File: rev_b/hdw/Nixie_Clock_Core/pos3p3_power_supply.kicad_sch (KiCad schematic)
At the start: 24 parts, among them Q401 BSS214NW, Q402 ZXMS6004FFTA, U401 LT8609A-DD

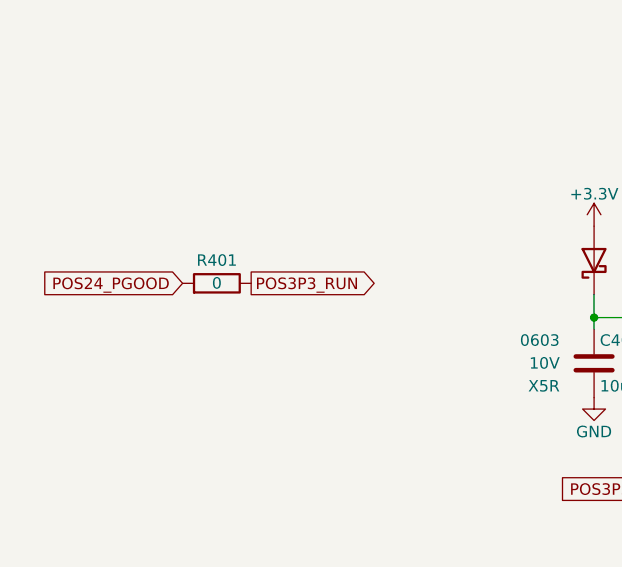
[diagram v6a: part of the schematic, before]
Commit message: added BOM
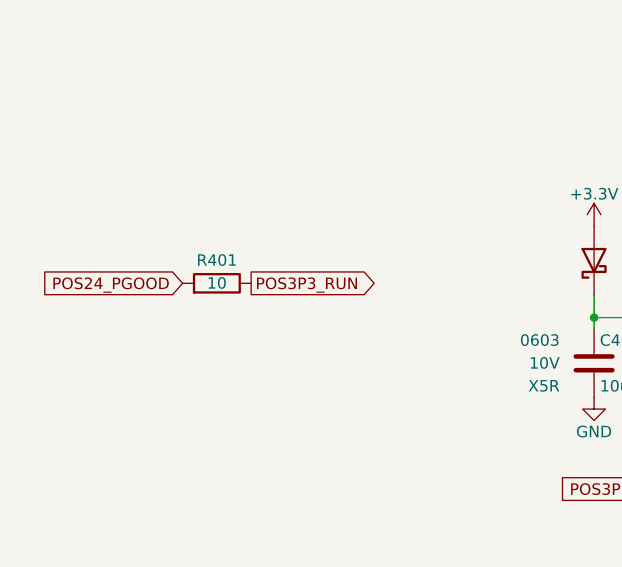
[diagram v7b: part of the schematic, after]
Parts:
- R401: value 0 -> 10; Digi-Key PN (none) -> 541-10.0HCT-ND
- R402, R404: Digi-Key PN (none) -> 541-10.0KHCT-ND
- R403: Digi-Key PN (none) -> 541-18.2KHCT-ND
- R405, R407: Digi-Key PN (none) -> 541-10.0HCT-ND
- R408: Digi-Key PN (none) -> 541-1.00MHCT-ND
- R409: Digi-Key PN (none) -> 541-309KHCT-ND
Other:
- title: (none) -> Nixie Clock Redux Core Board
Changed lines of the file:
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@@
   (paper "A")
   (title_block
-    (date "2023-05-12")
-    (rev "PRELIM")
+    (title "Nixie Clock Redux Core Board")
+    (date "2023-07-30")
+    (rev "B")
     (company "Drew Maatman")
   )
@@
     (stroke (width 0) (type default))
   )
-  (global_label "POS3P3_RUN" (shape input) (at 50.8 80.01 180)
+  (global_label "POS3P3_RUN" (shape input) (at 50.8 80.01 180) (fields_autoplaced)
     (effects (font (size 1.27 1.27)) (justify right))
-    (property "Intersheetrefs" "${INTERSHEET_REFS}" (at 50.8 80.01 0)
-      (effects (font (size 1.27 1.27)) hide)
-    )
-  )
-  (global_label "POS3P3_PGOOD" (shape output) (at 50.8 77.47 180)
+    (property "Intersheetrefs" "${INTERSHEET_REFS}" (at 35.4966 80.01 0)
+      (effects (font (size 1.27 1.27)) (justify right))
+    )
+  )
+  (global_label "POS3P3_PGOOD" (shape output) (at 50.8 77.47 180) (fields_autoplaced)
     (effects (font (size 1.27 1.27)) (justify right))
-    (property "Intersheetrefs" "${INTERSHEET_REFS}" (at 50.8 77.47 0)
-      (effects (font (size 1.27 1.27)) hide)
-    )
-  )
-  (global_label "POS24_PGOOD" (shape input) (at 43.18 166.37 180)
+    (property "Intersheetrefs" "${INTERSHEET_REFS}" (at 32.9566 77.47 0)
+      (effects (font (size 1.27 1.27)) (justify right))
+    )
+  )
+  (global_label "POS24_PGOOD" (shape input) (at 43.18 166.37 180) (fields_autoplaced)
     (effects (font (size 1.27 1.27)) (justify right))
-    (property "Intersheetrefs" "${INTERSHEET_REFS}" (at 43.18 166.37 0)
-      (effects (font (size 1.27 1.27)) hide)
-    )
-  )
-  (global_label "POS3P3_RUN" (shape input) (at 99.06 189.23 180)
+    (property "Intersheetrefs" "${INTERSHEET_REFS}" (at 26.6066 166.37 0)
+      (effects (font (size 1.27 1.27)) (justify right))
+    )
+  )
+  (global_label "POS3P3_RUN" (shape input) (at 99.06 189.23 180) (fields_autoplaced)
     (effects (font (size 1.27 1.27)) (justify right))
-    (property "Intersheetrefs" "${INTERSHEET_REFS}" (at 99.06 189.23 0)
-      (effects (font (size 1.27 1.27)) hide)
-    )
-  )
-  (global_label "POS3P3_SNS-" (shape passive) (at 203.2 54.61 90)
+    (property "Intersheetrefs" "${INTERSHEET_REFS}" (at 83.7566 189.23 0)
+      (effects (font (size 1.27 1.27)) (justify right))
+    )
+  )
+  (global_label "POS3P3_SNS-" (shape passive) (at 203.2 54.61 90) (fields_autoplaced)
     (effects (font (size 1.27 1.27)) (justify left))
-    (property "Intersheetrefs" "${INTERSHEET_REFS}" (at 203.2 54.61 0)
-      (effects (font (size 1.27 1.27)) hide)
-    )
-  )
-  (global_label "POS3P3_RUN" (shape output) (at 50.8 166.37 0)
+    (property "Intersheetrefs" "${INTERSHEET_REFS}" (at 203.2 39.027 90)
+      (effects (font (size 1.27 1.27)) (justify left))
+    )
+  )
+  (global_label "POS3P3_RUN" (shape output) (at 50.8 166.37 0) (fields_autoplaced)
     (effects (font (size 1.27 1.27)) (justify left))
-    (property "Intersheetrefs" "${INTERSHEET_REFS}" (at 50.8 166.37 0)
-      (effects (font (size 1.27 1.27)) hide)
-    )
-  )
-  (global_label "POS3P3_SNS+" (shape passive) (at 190.5 54.61 90)
+    (property "Intersheetrefs" "${INTERSHEET_REFS}" (at 66.1034 166.37 0)
+      (effects (font (size 1.27 1.27)) (justify left))
+    )
+  )
+  (global_label "POS3P3_SNS+" (shape passive) (at 190.5 54.61 90) (fields_autoplaced)
     (effects (font (size 1.27 1.27)) (justify left))
-    (property "Intersheetrefs" "${INTERSHEET_REFS}" (at 190.5 54.61 0)
-      (effects (font (size 1.27 1.27)) hide)
+    (property "Intersheetrefs" "${INTERSHEET_REFS}" (at 190.5 39.027 90)
+      (effects (font (size 1.27 1.27)) (justify left))
     )
   )
@@
       (effects (font (size 1.27 1.27)) (justify left))
     )
-    (property "Digi-Key PN" "" (at 114.3 165.1 0)
+    (property "Digi-Key PN" "541-10.0KHCT-ND" (at 114.3 165.1 0)
       (effects (font (size 1.524 1.524)) hide)
     )
@@
       (effects (font (size 1.27 1.27)) (justify left) hide)
     )
-    (property "Digi-Key PN" "" (at 215.9 76.2 0)
+    (property "Digi-Key PN" "541-1.00MHCT-ND" (at 215.9 76.2 0)
       (effects (font (size 1.524 1.524)) hide)
     )
@@
       (effects (font (size 1.27 1.27)) hide)
     )
-    (property "Digi-Key PN" "" (at 190.5 58.42 0)
+    (property "Digi-Key PN" "541-10.0HCT-ND" (at 190.5 58.42 0)
       (effects (font (size 1.27 1.27)) hide)
     )
@@
       (effects (font (size 1.27 1.27)) (justify left))
     )
-    (property "Digi-Key PN" "" (at 88.9 83.82 0)
+    (property "Digi-Key PN" "541-18.2KHCT-ND" (at 88.9 83.82 0)
       (effects (font (size 1.524 1.524)) hide)
     )
@@
       (effects (font (size 1.27 1.27)) (justify left) hide)
     )
-    (property "Digi-Key PN" "" (at 73.66 60.96 0)
+    (property "Digi-Key PN" "541-10.0KHCT-ND" (at 73.66 60.96 0)
       (effects (font (size 1.524 1.524)) hide)
     )
@@
       (effects (font (size 1.27 1.27)))
     )
-    (property "Value" "0" (at 46.99 166.37 90)
+    (property "Value" "10" (at 46.99 166.37 90)
       (effects (font (size 1.27 1.27)))
     )
@@
       (effects (font (size 1.27 1.27)) hide)
     )
-    (property "Digi-Key PN" "" (at 46.99 166.37 0)
+    (property "Digi-Key PN" "541-10.0HCT-ND" (at 46.99 166.37 0)
       (effects (font (size 1.27 1.27)) hide)
     )
@@
       (effects (font (size 1.27 1.27)) (justify left) hide)
     )
-    (property "Digi-Key PN" "" (at 215.9 99.06 0)
+    (property "Digi-Key PN" "541-309KHCT-ND" (at 215.9 99.06 0)
       (effects (font (size 1.524 1.524)) hide)
     )
@@
       (effects (font (size 1.27 1.27)) hide)
     )
-    (property "Digi-Key PN" "" (at 203.2 58.42 0)
-      (effects (font (size 1.27 1.27)) hide)
-    )
+    (property "Digi-Key PN" "541-10.0HCT-ND" (at 203.2 58.42 0)
+      (effects (font (size 1.27 1.27)) hide)
+    )
